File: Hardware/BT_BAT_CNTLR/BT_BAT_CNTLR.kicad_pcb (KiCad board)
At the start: 2 copper layers, 145 x 60 mm, 89 parts, among them J1 Barrel_Jack_Switch, J2 USB_A, J3 USB_A, J4 USB_A, J5 USB_A, J6 USB_A, J7 USB_A, J8 Conn_ARM_SWD_TagConnect_TC2030, U10 SN74LVC1T45DRL, U11 AP22814AW5, U12 SN74LVC1T45DRL, U13 AP22814AW5, U14 SN74LVC1T45DRL, U15 AP22814AW5, U2 LM1117DT-ADJ, U3 nRF52820-QDxx, U4 AP22814AW5, U5 SN74LVC1T45DRL, U6 SN74LVC1T45DRL, U7 AP22814AW5, U8 SN74LVC1T45DRL, U9 AP22814AW5, Y1 Crystal_GND24

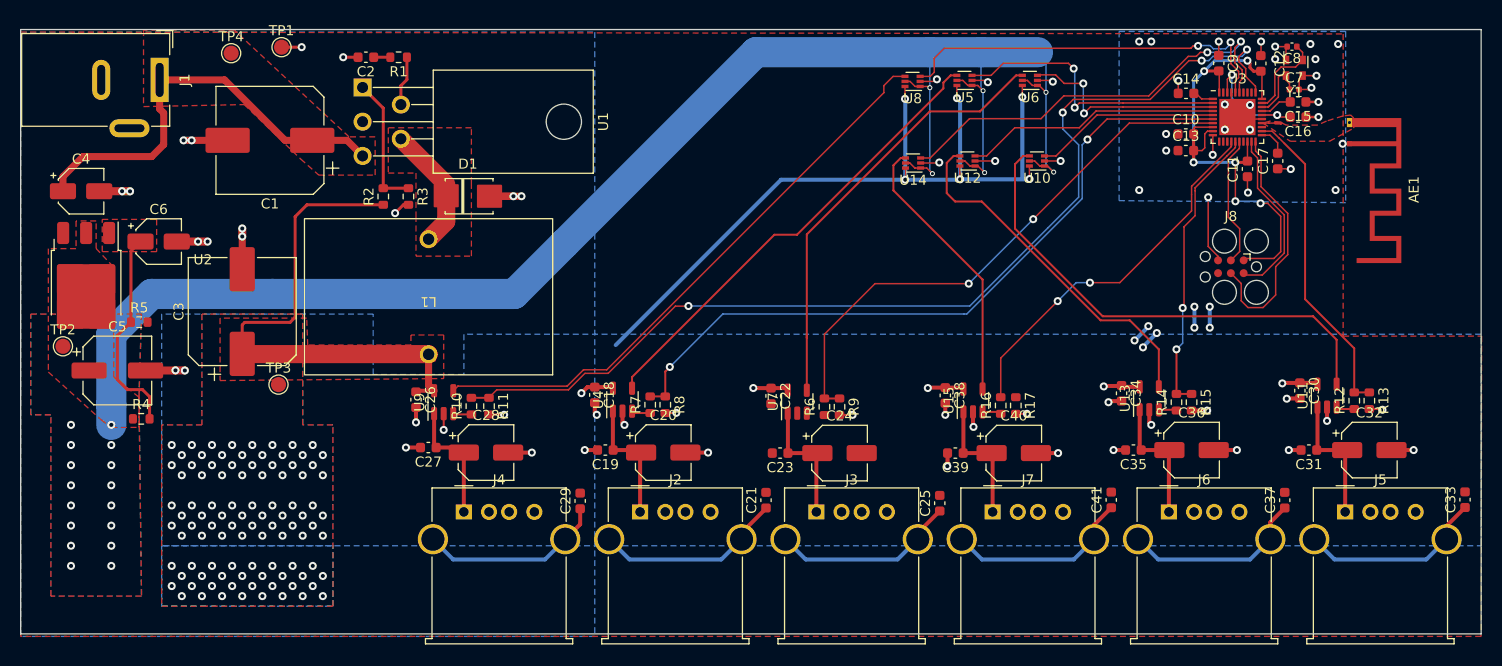
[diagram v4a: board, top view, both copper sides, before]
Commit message: routed
reorganized some components. traces  and vias need to be conforming. Silk needs to be reorganized.
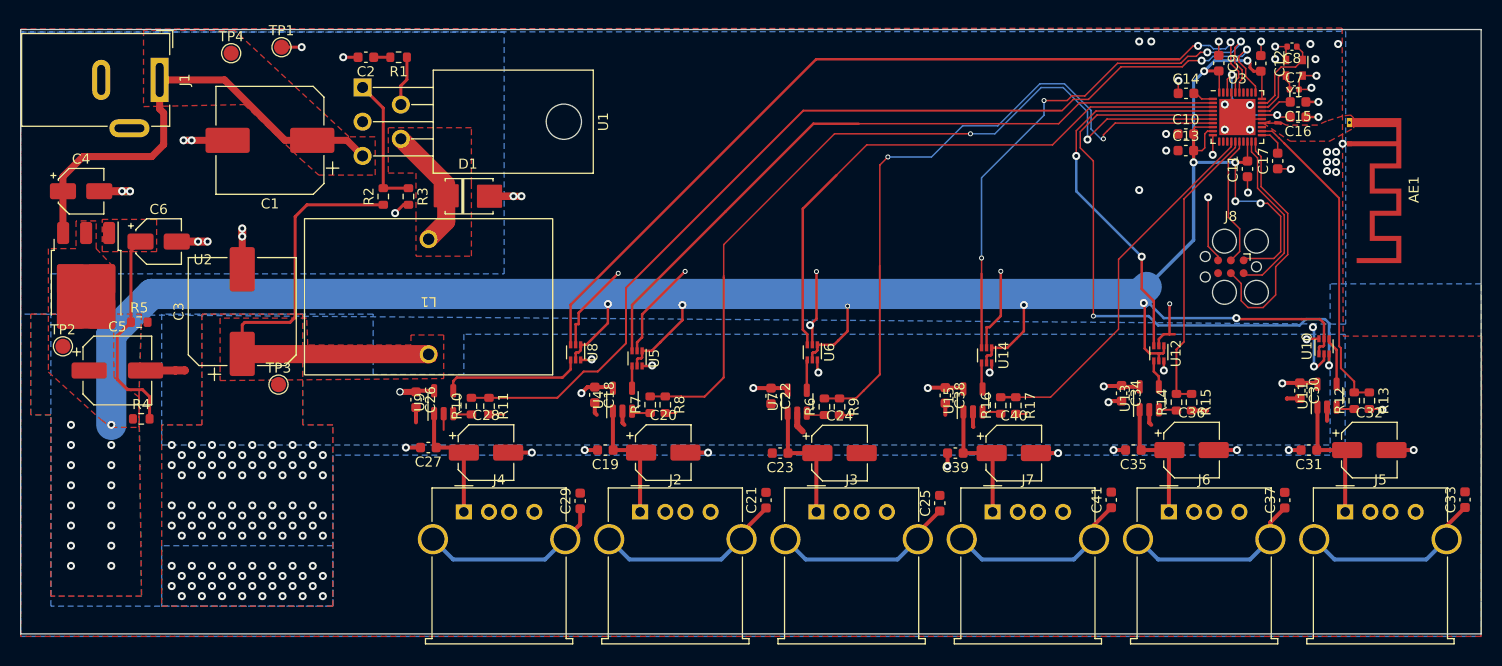
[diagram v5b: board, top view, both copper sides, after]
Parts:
- moved U8 42.9 mm to (96.1, 65.8), turned to -90 degrees
- moved U5 42.6 mm to (102.2, 66.4), turned to -90 degrees
- moved U6 34.6 mm to (119.6, 65.8), turned to -90 degrees
- moved U10 33.9 mm to (170.4, 65.2), turned to 90 degrees
- moved U12 26.9 mm to (154.0, 65.9), turned to -90 degrees
- moved U14 20.4 mm to (136.9, 66.1), turned to -90 degrees
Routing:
- net 5V_5A: track 150.7 -> 74.7 mm, vias 107 -> 108
- net /USB connectors+load switches/EN_3: track 38.9 -> 86.1 mm
- net /USB connectors+load switches/EN6: track 49.1 -> 4.82 mm
- net /USB connectors+load switches/EN3: track 58.2 -> 14.0 mm
- net /USB connectors+load switches/EN1: track 46.1 -> 2.21 mm
- net /USB connectors+load switches/EN_6: track 18.4 -> 62.3 mm, vias 0 -> 2
- net /USB connectors+load switches/EN_1: track 28.6 -> 70.5 mm, vias 2 -> 0
- net /USB connectors+load switches/EN2: track 43.7 -> 3.03 mm
- net /USB connectors+load switches/EN_2: track 21.0 -> 58.6 mm, vias 2 -> 0
- net /USB connectors+load switches/EN5: track 35.8 -> 2.78 mm
- net GND: track 120.6 -> 150.2 mm, vias 82 -> 65
- net /USB connectors+load switches/EN4: track 27.4 -> 2.63 mm
- net +3V3: track 222.9 -> 247.4 mm
- net /USB connectors+load switches/EN_5: track 25.5 -> 38.9 mm, vias 0 -> 2
- net /USB connectors+load switches/FLT_2: track 55.1 -> 67.9 mm
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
